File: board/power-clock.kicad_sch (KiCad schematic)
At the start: 9 parts, among them SW1 RESET, Y1 12 MHz

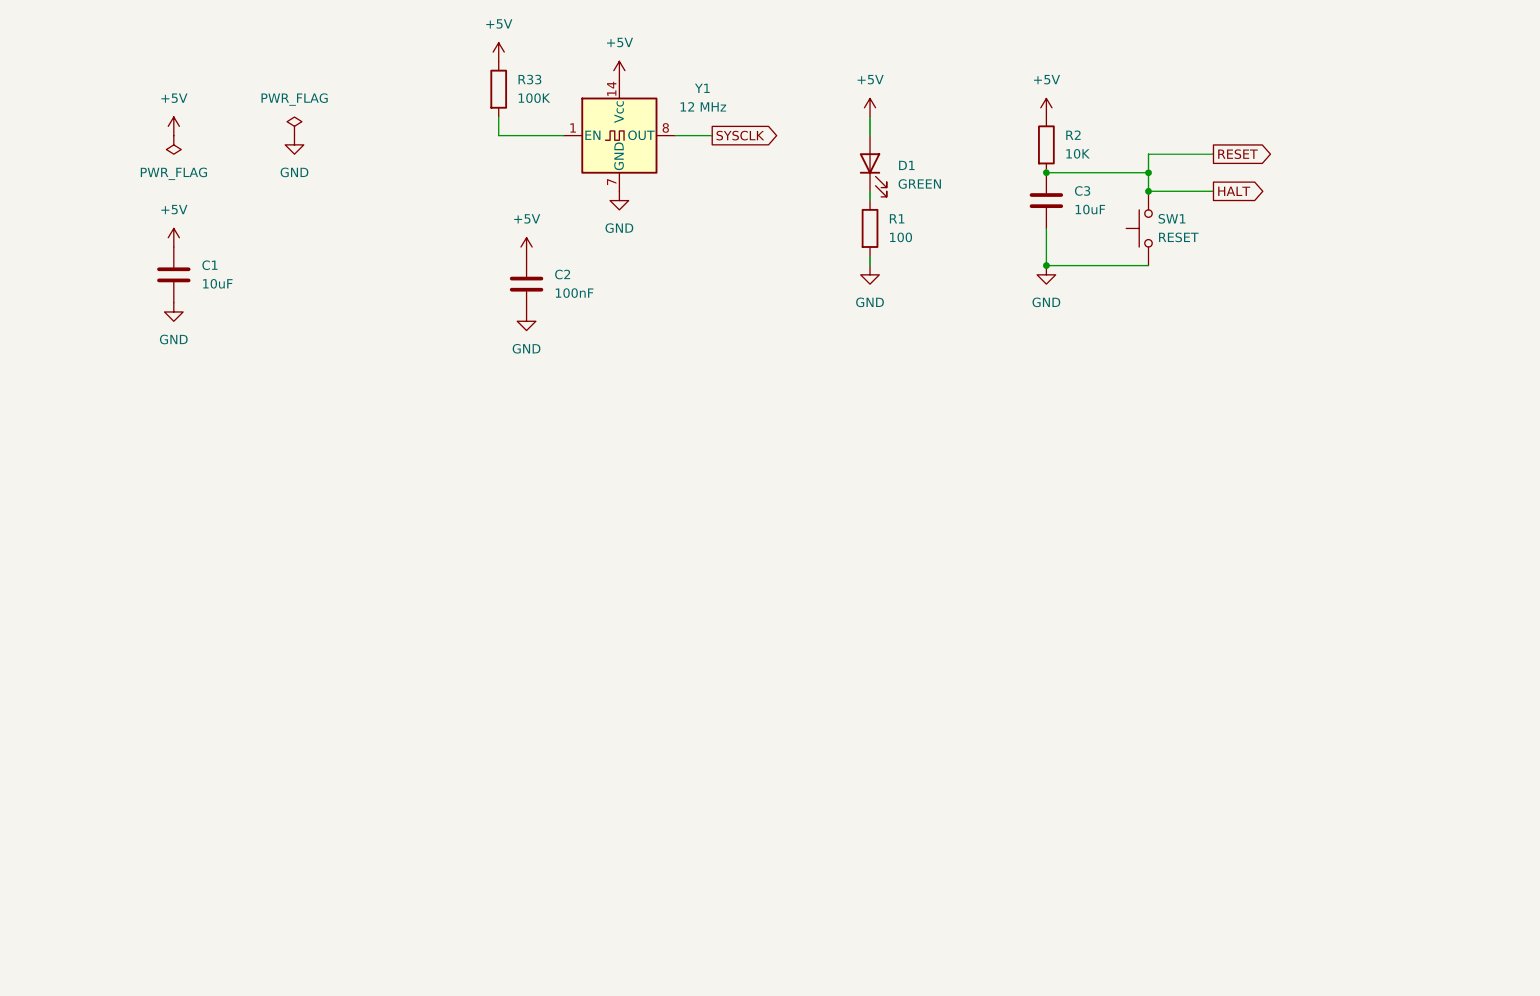
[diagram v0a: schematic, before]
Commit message: change IO to 8051 variant, add audio
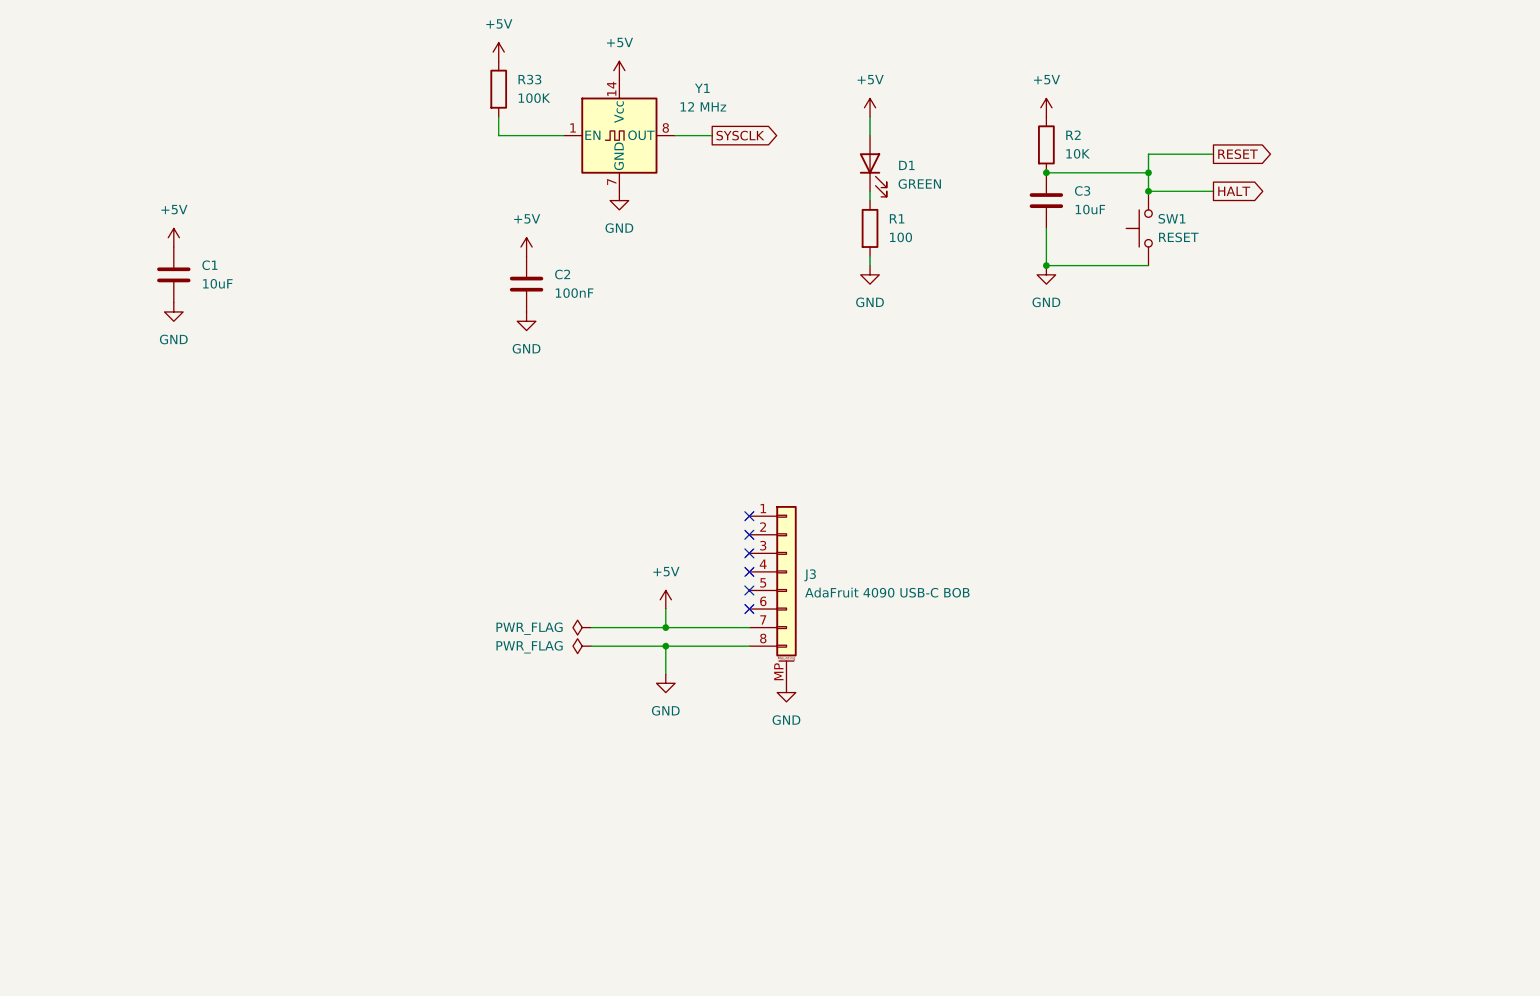
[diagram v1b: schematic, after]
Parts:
- added J3: AdaFruit 4090 USB-C BOB, symbol Connector_Generic_MountingPin:Conn_01x08_MountingPin
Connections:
- net +5V: now also J3.7 (Pin_7)
- net GND: now also J3.8 (Pin_8), J3.MP (MountPin)
- no-connect marks 0 -> 6

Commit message: design draft complete, added footprints
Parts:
- C1, C3: footprint (none) -> Capacitor_THT:CP_Radial_D5.0mm_P2.50mm
- C2: footprint (none) -> Capacitor_THT:C_Disc_D5.0mm_W2.5mm_P5.00mm
- J3: footprint (none) -> Connector_PinHeader_2.54mm:PinHeader_1x08_P2.54mm_Vertical
- R1, R2, R33: footprint (none) -> Resistor_THT:R_Axial_DIN0207_L6.3mm_D2.5mm_P10.16mm_Horizontal
- SW1: footprint (none) -> Button_Switch_THT:SW_TH_Tactile_Omron_B3F-106x
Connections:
- net HALT renamed ~{RESET}
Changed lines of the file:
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@@
 	(paper "A4")
-	(junction
-		(at 173.99 45.72)
-		(diameter 0)
-		(color 0 0 0 0)
-	)
 	(junction
 		(at 107.95 107.95)
@@
 	(wire
 		(pts
-			(xy 182.88 45.72) (xy 173.99 45.72)
+			(xy 160.02 55.88) (xy 173.99 55.88)
 		)
 		(stroke
@@
 	(wire
 		(pts
-			(xy 160.02 55.88) (xy 173.99 55.88)
+			(xy 160.02 43.18) (xy 173.99 43.18)
 		)
 		(stroke
@@
 	(wire
 		(pts
-			(xy 160.02 43.18) (xy 173.99 43.18)
+			(xy 160.02 50.8) (xy 160.02 55.88)
 		)
 		(stroke
@@
 	(wire
 		(pts
-			(xy 160.02 50.8) (xy 160.02 55.88)
+			(xy 107.95 107.95) (xy 107.95 111.76)
 		)
 		(stroke
@@
 		)
 	)
-	(wire
-		(pts
-			(xy 107.95 107.95) (xy 107.95 111.76)
-		)
-		(stroke
-			(width 0)
-			(type default)
-		)
-	)
-	(global_label "HALT"
+	(global_label "~{RESET}"
 		(shape output)
-		(at 182.88 45.72 0)
+		(at 182.88 40.64 0)
 		(fields_autoplaced yes)
 		(effects
@@
 		)
 		(property "Intersheetrefs" "${INTERSHEET_REFS}"
-			(at 190.28 45.72 0)
+			(at 191.6103 40.64 0)
 			(effects
 				(font
@@
 		)
 	)
-	(global_label "RESET"
+	(global_label "SYSCLK"
 		(shape output)
-		(at 182.88 40.64 0)
+		(at 114.3 38.1 0)
 		(fields_autoplaced yes)
 		(effects
@@
 		)
 		(property "Intersheetrefs" "${INTERSHEET_REFS}"
-			(at 191.6103 40.64 0)
-			(effects
-				(font
-					(size 1.27 1.27)
-				)
-				(justify left)
-				(hide yes)
-			)
-		)
-	)
-	(global_label "SYSCLK"
-		(shape output)
-		(at 114.3 38.1 0)
-		(fields_autoplaced yes)
-		(effects
-			(font
-				(size 1.27 1.27)
-			)
-			(justify left)
-		)
-		(property "Intersheetrefs" "${INTERSHEET_REFS}"
 			(at 124.3609 38.1 0)
 			(effects
@@
 			)
 		)
-		(property "Footprint" ""
+		(property "Footprint" "Resistor_THT:R_Axial_DIN0207_L6.3mm_D2.5mm_P10.16mm_Horizontal"
 			(at 134.112 50.8 90)
 			(effects
@@
 			)
 		)
-		(property "Footprint" ""
+		(property "Footprint" "Capacitor_THT:CP_Radial_D5.0mm_P2.50mm"
 			(at 160.9852 50.8 0)
 			(effects
@@
 			)
 		)
-		(property "Footprint" ""
+		(property "Footprint" "Button_Switch_THT:SW_TH_Tactile_Omron_B3F-106x"
 			(at 168.91 50.8 0)
 			(effects
@@
 			)
 		)
-		(property "Description" "Push button switch, generic, two pins"
+		(property "Description" "Push button switch, generic, two pins - https://www.digikey.com/en/products/detail/omron-electronics-inc-emc-div/B3F-1060/1811725"
 			(at 173.99 50.8 0)
 			(effects
@@
 			)
 		)
-		(property "Footprint" ""
+		(property "Footprint" "Resistor_THT:R_Axial_DIN0207_L6.3mm_D2.5mm_P10.16mm_Horizontal"
 			(at 158.242 39.37 90)
 			(effects
@@
 			)
 		)
-		(property "Footprint" ""
+		(property "Footprint" "Capacitor_THT:C_Disc_D5.0mm_W2.5mm_P5.00mm"
 			(at 89.8652 62.23 0)
 			(effects
@@
 			)
 		)
-		(property "Footprint" ""
+		(property "Footprint" "Capacitor_THT:CP_Radial_D5.0mm_P2.50mm"
 			(at 41.6052 60.96 0)
 			(effects
@@
 			)
 		)
-		(property "Footprint" ""
+		(property "Footprint" "Connector_PinHeader_2.54mm:PinHeader_1x08_P2.54mm_Vertical"
 			(at 124.46 97.79 0)
 			(effects
@@
 			)
 		)
-		(property "Footprint" ""
+		(property "Footprint" "Resistor_THT:R_Axial_DIN0207_L6.3mm_D2.5mm_P10.16mm_Horizontal"
 			(at 83.312 31.75 90)
 			(effects

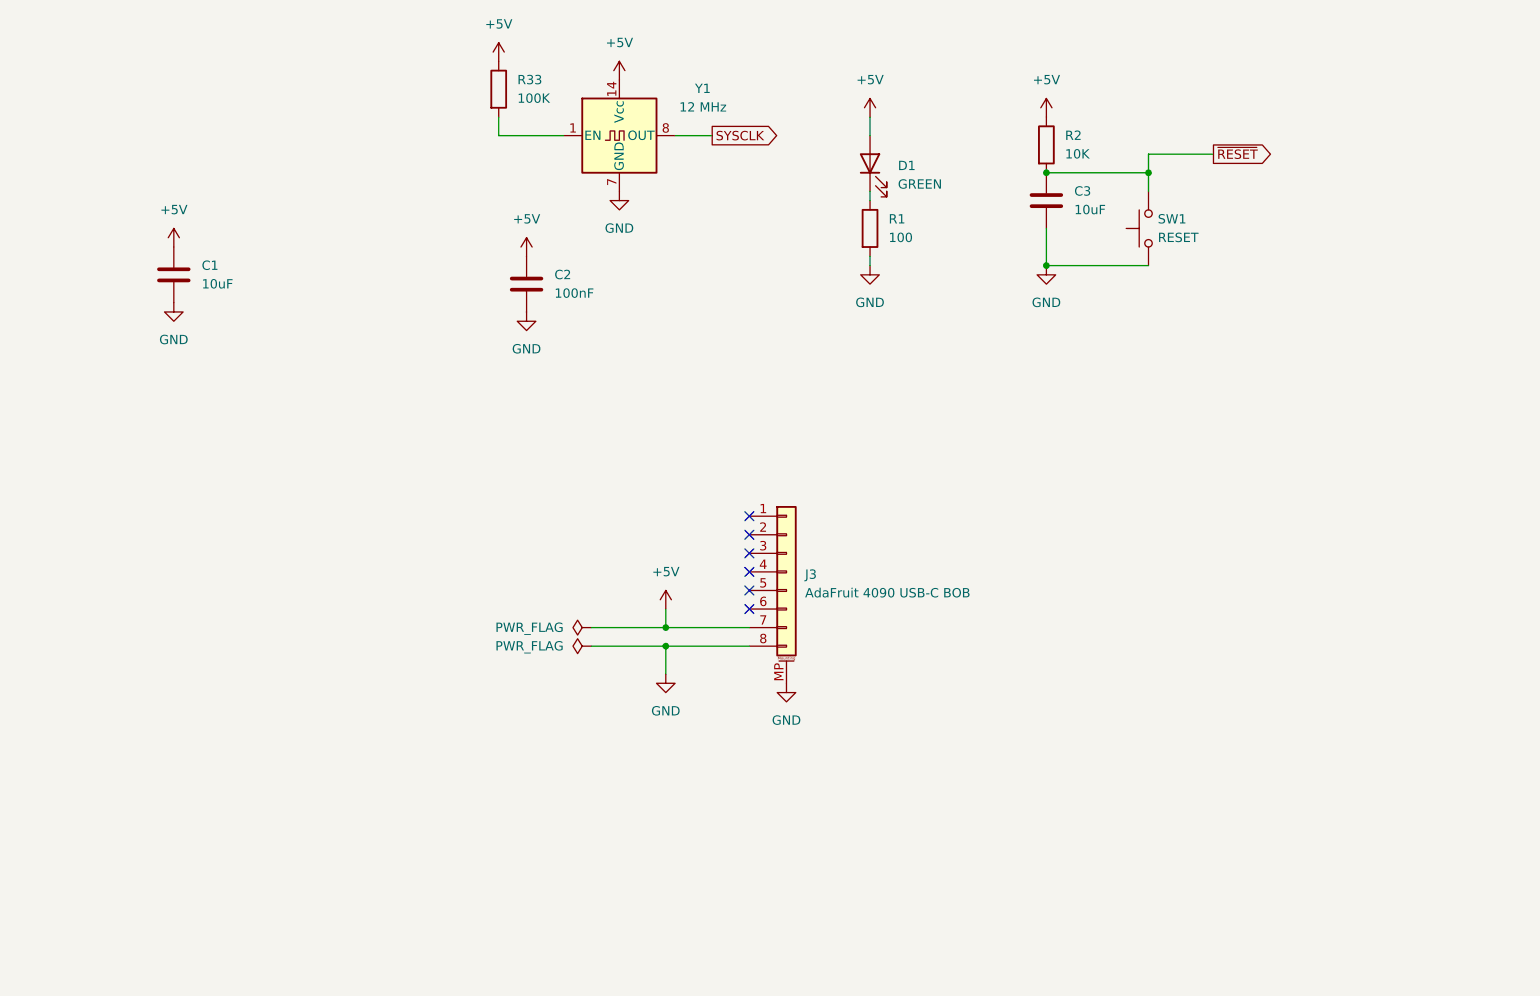
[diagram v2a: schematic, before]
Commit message: start of PCB and MMU
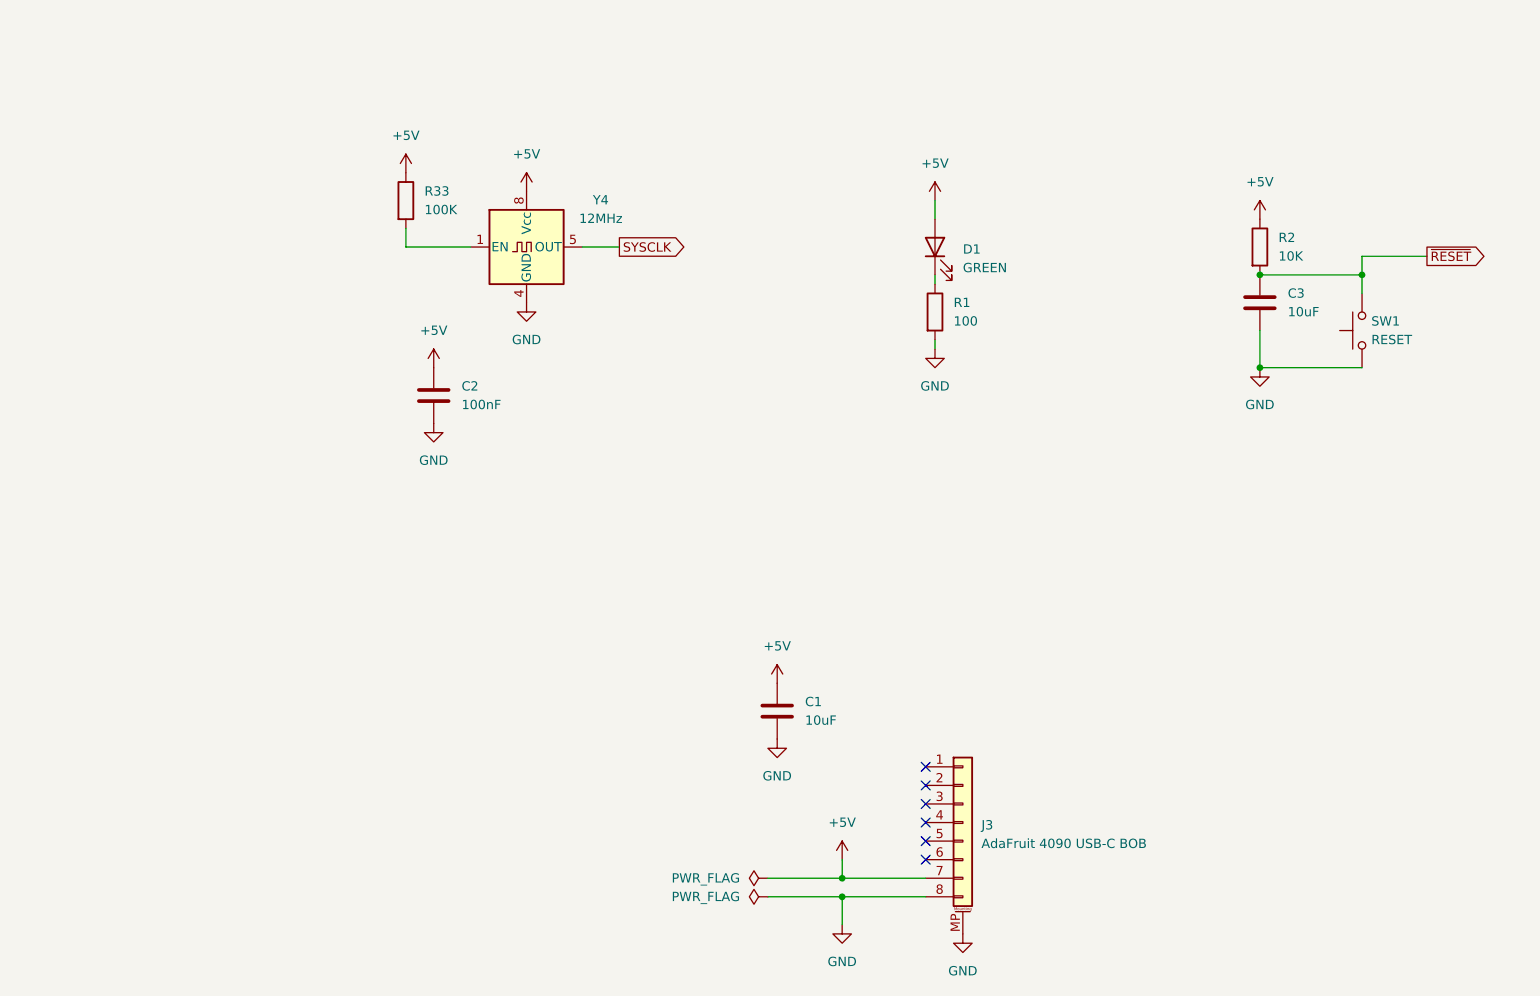
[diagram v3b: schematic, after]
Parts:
- removed Y1: 12 MHz, Oscillator:Oscillator_DIP-14, symbol Oscillator:CXO_DIP14
- added Y4: 12MHz, Oscillator:Oscillator_DIP-8, symbol Oscillator:CXO_DIP8
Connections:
- net +5V: now also Y4.8 (Vcc)
- net GND: now also Y4.4 (GND)
- net SYSCLK: now also Y4.5 (OUT)
- net at R33.2: now also Y4.1 (EN)
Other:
- moved on the sheet: C1, C2, C3, D1, J3, R1, R2, R33, SW1

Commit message: checkpoint
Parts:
- added H1, H2, H3, H4, H9: MountingHole_Pad, MountingHole:MountingHole_2.5mm_Pad, symbol Mechanical:MountingHole_Pad
- J3: symbol Connector_Generic_MountingPin:Conn_01x08_MountingPin -> Connector_Generic:Conn_01x08
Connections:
- net GND: now also H1.1, H2.1, H3.1, H4.1, H9.1; no longer J3.MP (MountPin)

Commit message: checkpoint before reordering 1508 inputs
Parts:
- H1, H2, H3, H4, H9: footprint MountingHole:MountingHole_2.5mm_Pad -> MountingHole:MountingHole_2.5mm_Pad_Via
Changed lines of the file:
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@@
 			)
 		)
-		(property "Footprint" "MountingHole:MountingHole_2.5mm_Pad"
+		(property "Footprint" "MountingHole:MountingHole_2.5mm_Pad_Via"
 			(at 30.48 128.27 0)
 			(effects
@@
 			)
 		)
-		(property "Footprint" "MountingHole:MountingHole_2.5mm_Pad"
+		(property "Footprint" "MountingHole:MountingHole_2.5mm_Pad_Via"
 			(at 30.48 138.43 0)
 			(effects
@@
 			)
 		)
-		(property "Footprint" "MountingHole:MountingHole_2.5mm_Pad"
+		(property "Footprint" "MountingHole:MountingHole_2.5mm_Pad_Via"
 			(at 30.48 97.79 0)
 			(effects
@@
 			)
 		)
-		(property "Footprint" "MountingHole:MountingHole_2.5mm_Pad"
+		(property "Footprint" "MountingHole:MountingHole_2.5mm_Pad_Via"
 			(at 30.48 118.11 0)
 			(effects
@@
 			)
 		)
-		(property "Footprint" "MountingHole:MountingHole_2.5mm_Pad"
+		(property "Footprint" "MountingHole:MountingHole_2.5mm_Pad_Via"
 			(at 30.48 107.95 0)
 			(effects

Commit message: checkpoint
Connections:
- net SYSCLK renamed CPUCLK
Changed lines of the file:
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@@
 		)
 	)
-	(global_label "SYSCLK"
+	(global_label "CPUCLK"
 		(shape output)
 		(at 101.6 53.34 0)

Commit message: Board rev1 PCB complete, already have a spot fix
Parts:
- H1, H2, H3, H4, H9: value MountingHole_Pad -> MountingHole
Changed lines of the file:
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@@
 			)
 		)
-		(property "Value" "MountingHole_Pad"
+		(property "Value" "MountingHole"
 			(at 29.21 124.46 90)
 			(effects
@@
 			)
 		)
-		(property "Value" "MountingHole_Pad"
+		(property "Value" "MountingHole"
 			(at 29.21 134.62 90)
 			(effects
@@
 			)
 		)
-		(property "Value" "MountingHole_Pad"
+		(property "Value" "MountingHole"
 			(at 29.21 93.98 90)
 			(effects
@@
 			)
 		)
-		(property "Value" "MountingHole_Pad"
+		(property "Value" "MountingHole"
 			(at 29.21 114.3 90)
 			(effects
@@
 			)
 		)
-		(property "Value" "MountingHole_Pad"
+		(property "Value" "MountingHole"
 			(at 29.21 104.14 90)
 			(effects
